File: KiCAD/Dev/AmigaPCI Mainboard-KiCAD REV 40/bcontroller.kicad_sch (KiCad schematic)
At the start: 32 parts, among them CN409 SPI, J901 IDE MODES, U111 74LVC16646, U112 74LVC16646, U409 ICE40HX4K-TQ144, U409F1 W25X20CLSN

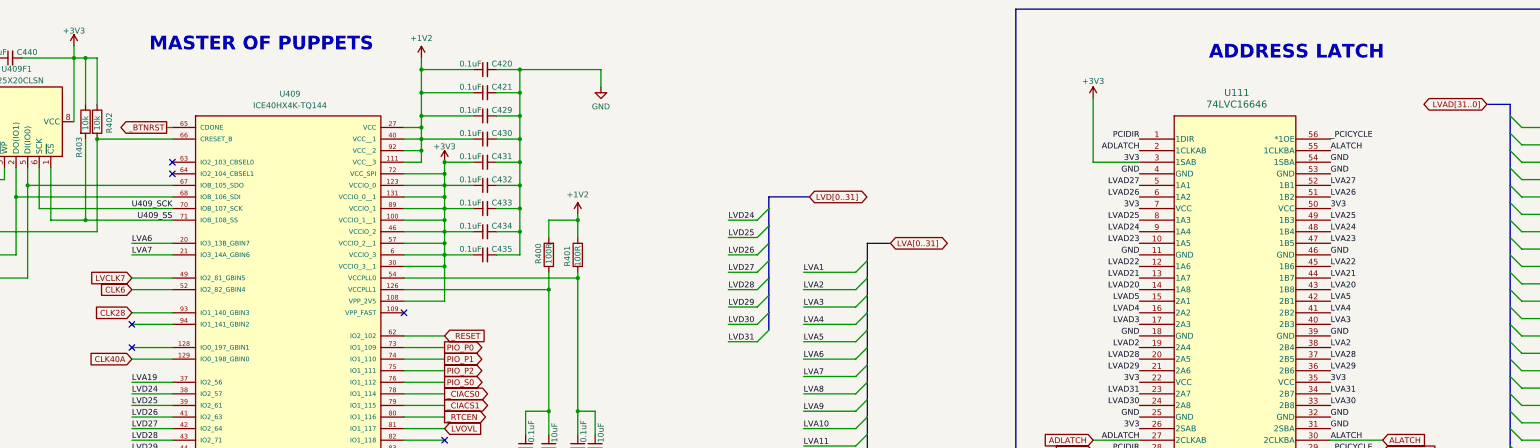
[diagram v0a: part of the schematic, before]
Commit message: Schematic Changes to Clocks 09-JUL-2024
Make changes to support clock generation on CPU local bus card.
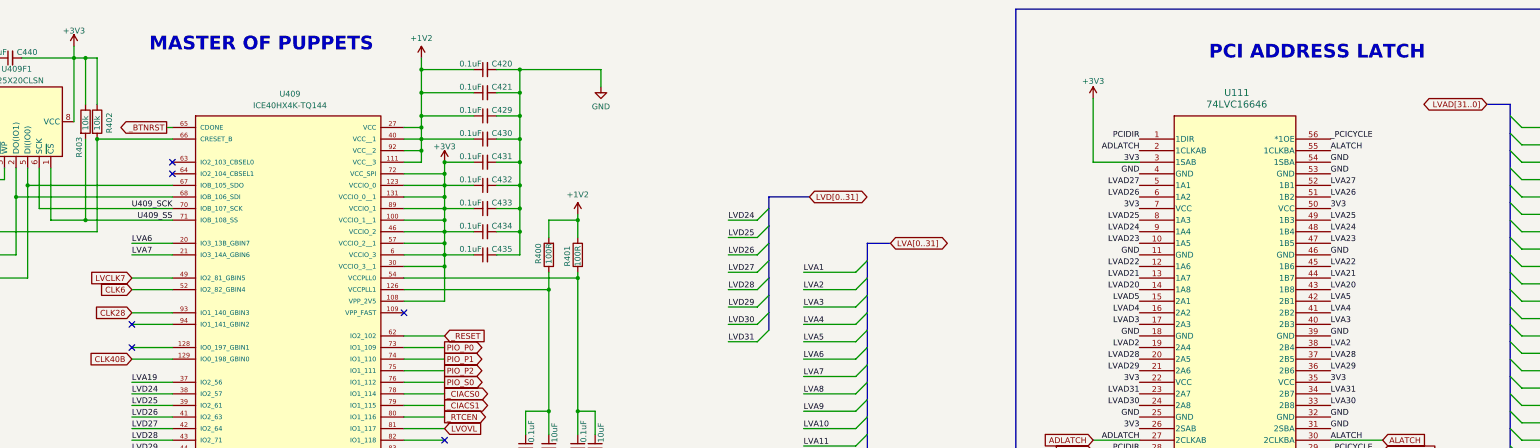
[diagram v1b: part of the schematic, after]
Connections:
- net CLK40A renamed CLK40B
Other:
- note added: "PCI ADDRESS LATCH"
- note removed: "ADDRESS LATCH"
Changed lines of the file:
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@@
 	(title_block
 		(title "AMIGA PCI")
-		(date "2024-07-03")
+		(date "2024-07-09")
 		(rev "4.0")
 	)
@@
 		)
 	)
-	(text "ADDRESS LATCH"
+	(text "PCI ADDRESS LATCH"
 		(exclude_from_sim no)
 		(at 314.96 33.528 0)
@@
 		)
 	)
-	(global_label "CLK40A"
+	(global_label "CLK40B"
 		(shape input)
 		(at 78.74 99.06 180)
@@
 		)
 		(property "Intersheetrefs" "${INTERSHEET_REFS}"
-			(at 68.6791 99.06 0)
+			(at 68.4977 99.06 0)
 			(effects
 				(font

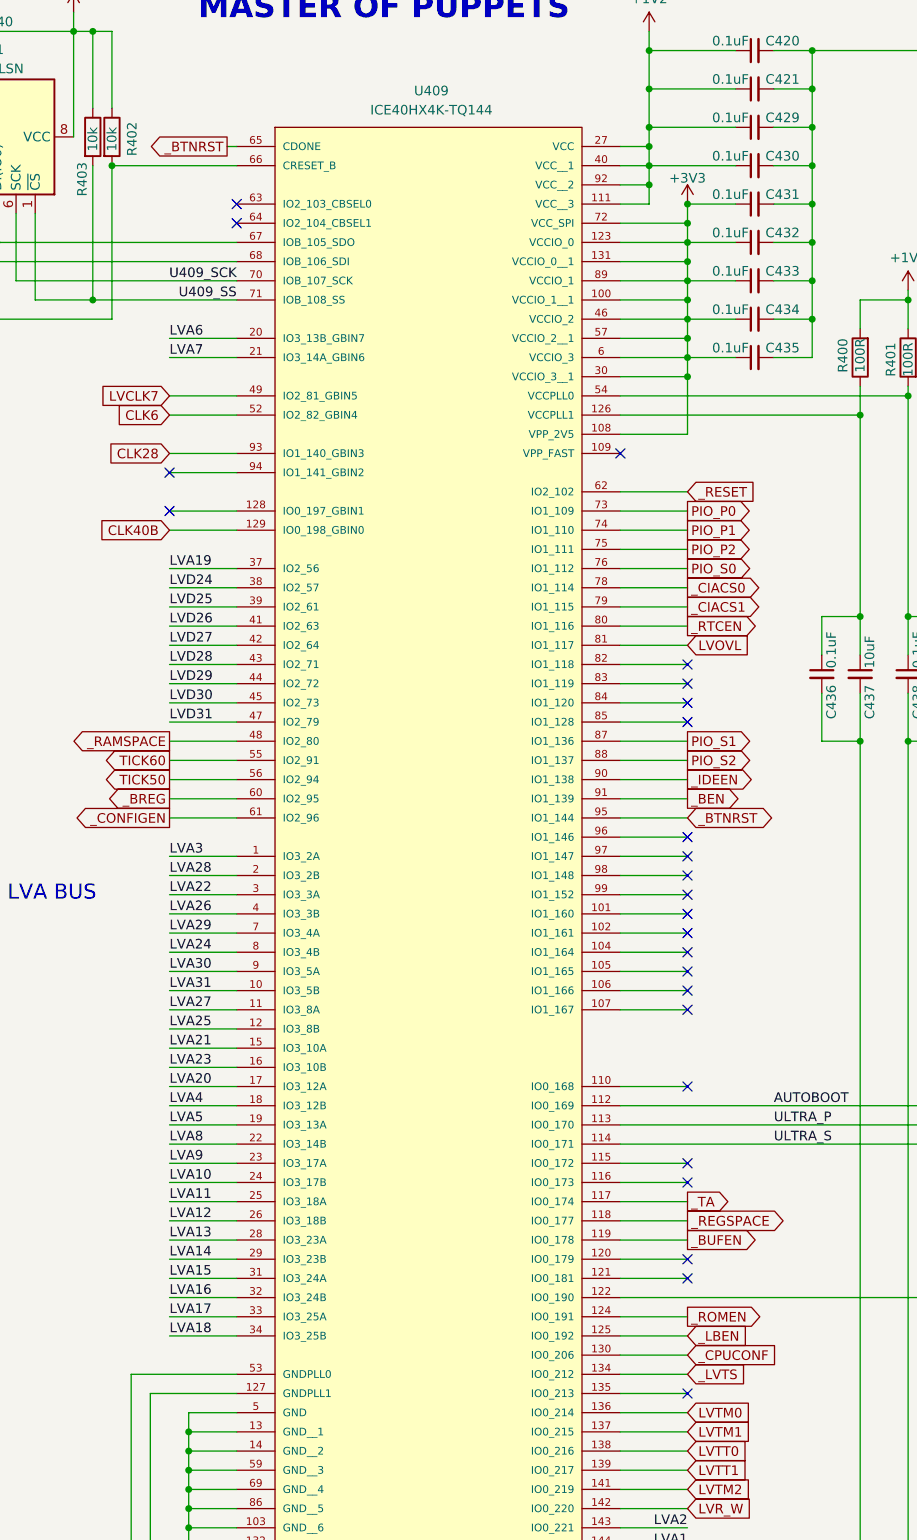
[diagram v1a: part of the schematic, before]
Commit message: AmigaPCI Rev 4.0 Schematic Updates 17-JUL-2024
Changed reset circuit, added _DSACKx, Dropped _LOCKE from Local Bus Port,  added CPU Reset In to Local Bus Port.
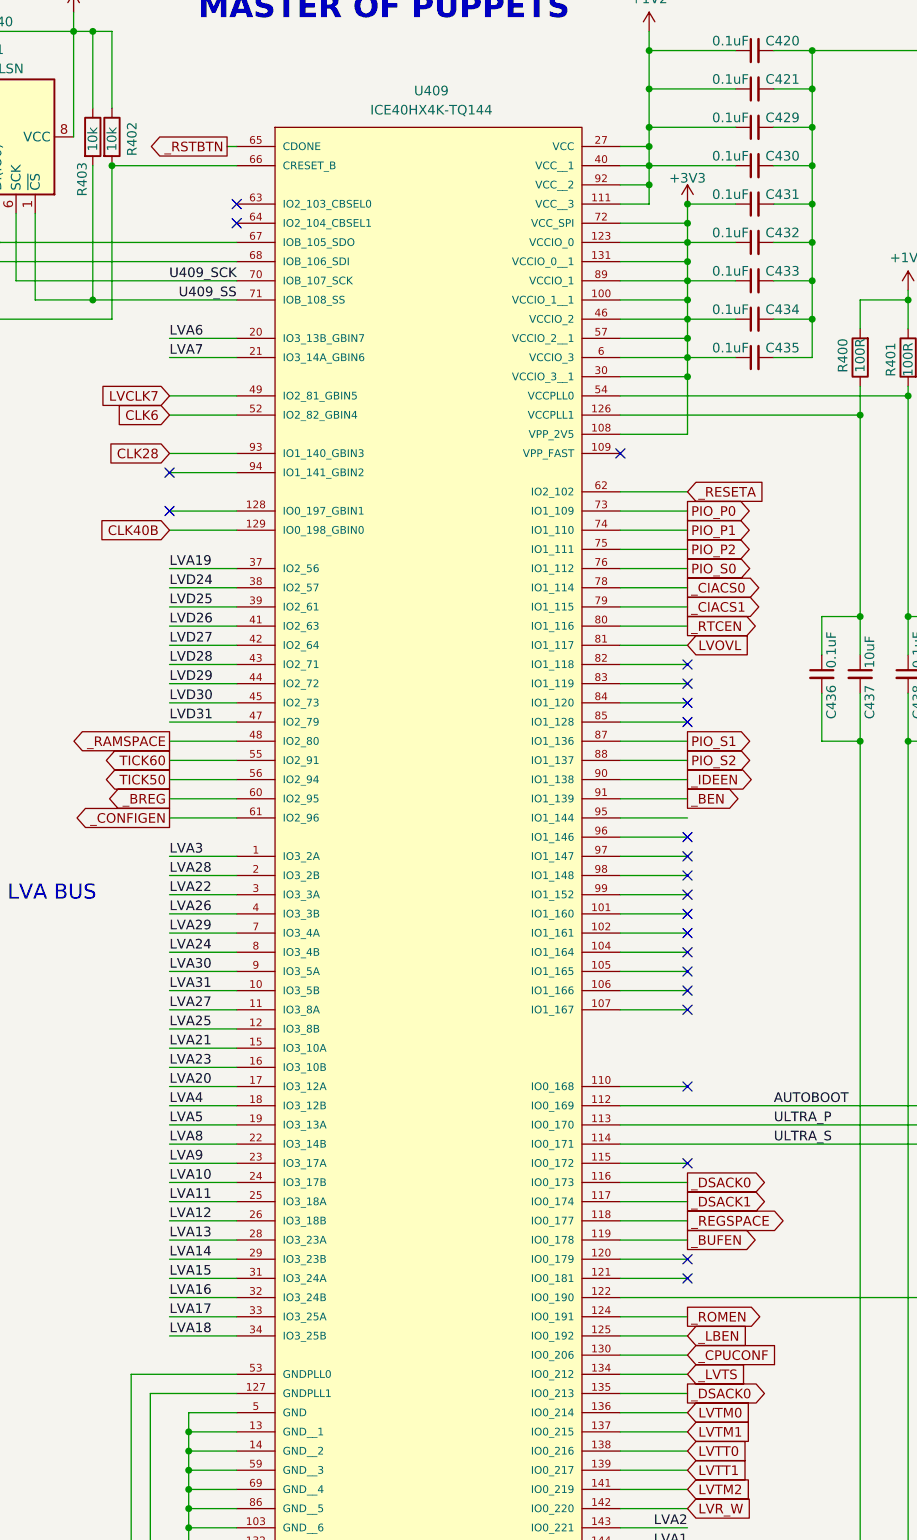
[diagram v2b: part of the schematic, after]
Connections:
- net _DSACK0: now reaches U409.116 (IO0_173)
- net _DSACK0: now also U409.135 (IO0_213)
- net _BTNRST: no longer names the net of U409.95 (IO1_144)
- net _BTNRST: no longer U409.65 (CDONE)
- net _RESET renamed _RESETA
- net _TA renamed _DSACK1
- new net _RSTBTN: U409.65 (CDONE)
- no-connect marks 29 -> 27
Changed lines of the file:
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@@
 	(title_block
 		(title "AMIGA PCI")
-		(date "2024-07-09")
+		(date "2024-07-17")
 		(rev "4.0")
 	)
@@
 	)
 	(no_connect
-		(at 147.32 185.42)
-	)
-	(no_connect
 		(at 147.32 152.4)
 	)
@@
 	)
 	(no_connect
-		(at 147.32 213.36)
-	)
-	(no_connect
 		(at 87.63 58.42)
 	)
@@
 		)
 	)
-	(global_label "_RESET"
+	(global_label "_RESETA"
 		(shape input)
 		(at 147.32 93.98 0)
@@
 		)
 	)
+	(global_label "_DSACK0"
+		(shape output)
+		(at 147.32 213.36 0)
+		(fields_autoplaced yes)
+		(effects
+			(font
+				(size 1.27 1.27)
+			)
+			(justify left)
+		)
+		(property "Intersheetrefs" "${INTERSHEET_REFS}"
+			(at 158.5904 213.36 0)
+			(effects
+				(font
+					(size 1.27 1.27)
+				)
+				(justify left)
+			)
+		)
+	)
 	(global_label "_CPUCONF"
 		(shape input)
@@
 		)
 	)
+	(global_label "_DSACK0"
+		(shape output)
+		(at 147.32 185.42 0)
+		(fields_autoplaced yes)
+		(effects
+			(font
+				(size 1.27 1.27)
+			)
+			(justify left)
+		)
+		(property "Intersheetrefs" "${INTERSHEET_REFS}"
+			(at 158.5904 185.42 0)
+			(effects
+				(font
+					(size 1.27 1.27)
+				)
+				(justify left)
+			)
+		)
+	)
 	(global_label "LVCLK7"
 		(shape input)
@@
 		)
 	)
-	(global_label "_TA"
+	(global_label "_DSACK1"
 		(shape output)
 		(at 147.32 187.96 0)
@@
 		)
 		(property "Intersheetrefs" "${INTERSHEET_REFS}"
-			(at 153.329 187.96 0)
+			(at 158.5904 187.96 0)
 			(effects
 				(font
@@
 		)
 	)
-	(global_label "_BTNRST"
-		(shape bidirectional)
-		(at 147.32 137.16 0)
-		(effects
-			(font
-				(size 1.27 1.27)
-			)
-			(justify left)
-		)
-		(property "Intersheetrefs" "${INTERSHEET_REFS}"
-			(at 158.242 137.16 0)
-			(effects
-				(font
-					(size 1.27 1.27)
-				)
-				(justify left)
-			)
-		)
-	)
 	(global_label "_IDEEN"
 		(shape output)
@@
 		)
 	)
-	(global_label "_BTNRST"
+	(global_label "_RSTBTN"
 		(shape output)
 		(at 86.36 48.26 180)

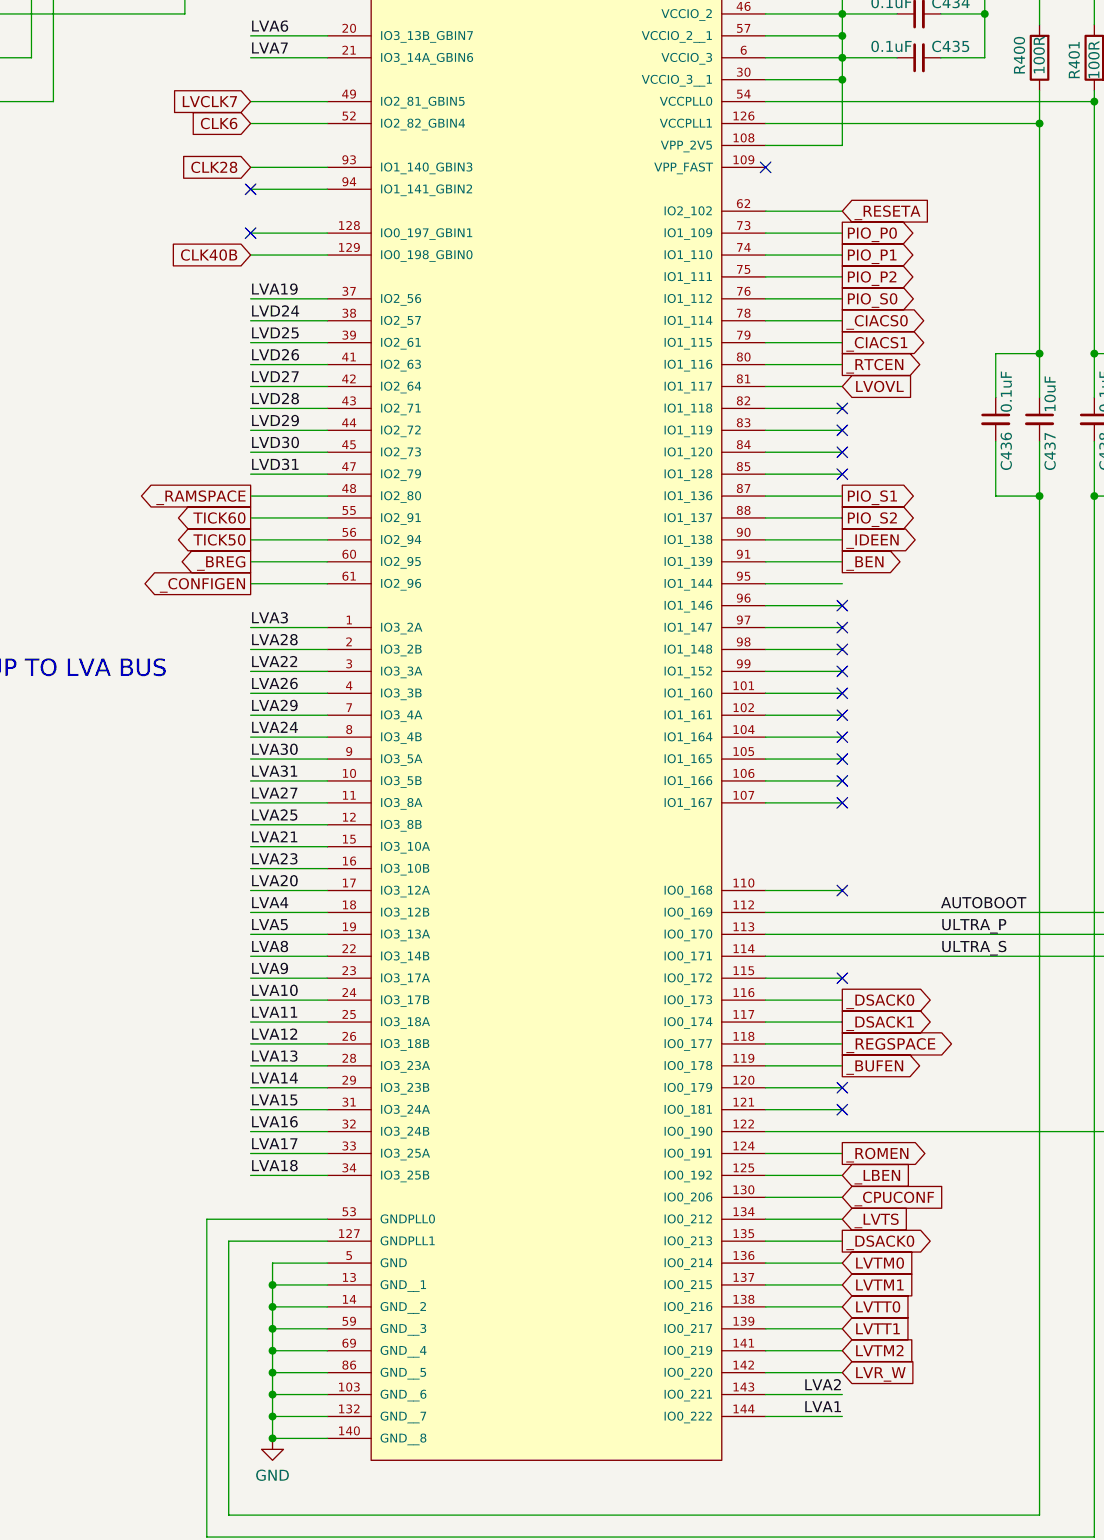
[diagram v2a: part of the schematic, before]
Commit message: AmigaPCI Rev 4.0 Routing
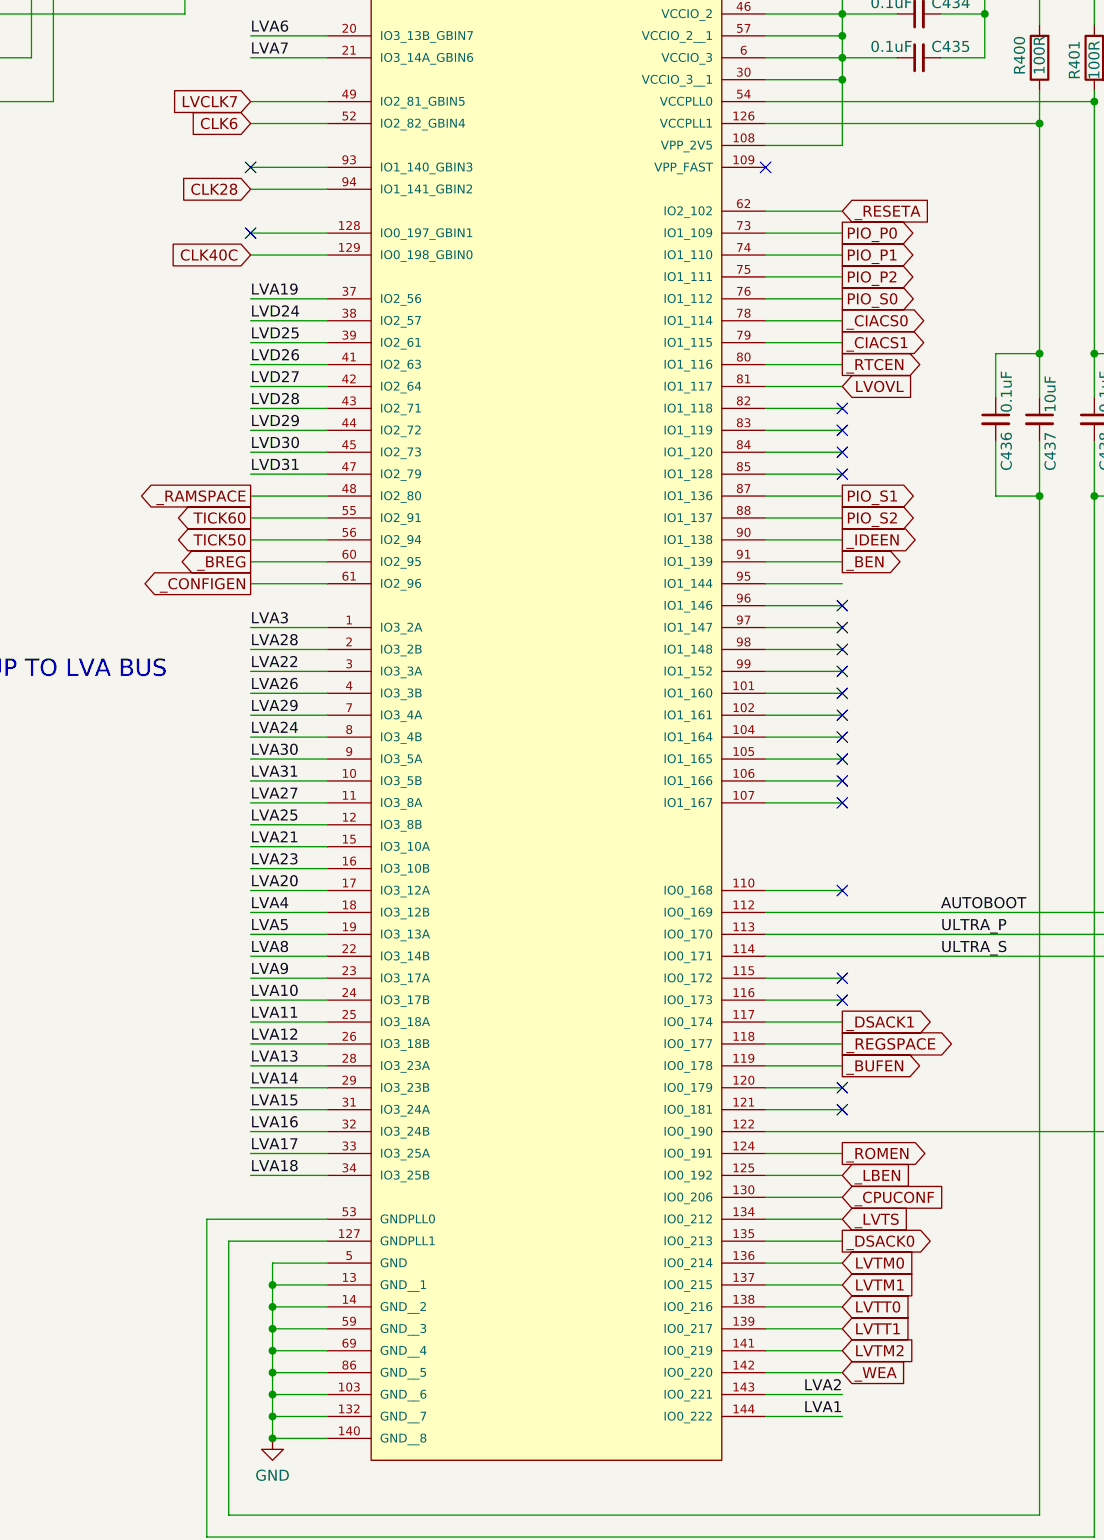
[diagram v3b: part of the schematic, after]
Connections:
- net CLK28: now also U409.94 (IO1_141_GBIN2); no longer U409.93 (IO1_140_GBIN3)
- net _DSACK0: no longer U409.116 (IO0_173)
- net CLK40B renamed CLK40C
- net LVR_W renamed _WEA
- no-connect marks 27 -> 28
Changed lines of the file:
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@@
 	)
 	(no_connect
+		(at 147.32 185.42)
+	)
+	(no_connect
 		(at 147.32 162.56)
 	)
@@
 	)
 	(no_connect
-		(at 78.74 91.44)
+		(at 78.74 88.9)
 	)
 	(no_connect
@@
 		)
 	)
-	(global_label "CLK40B"
+	(global_label "CLK40C"
 		(shape input)
 		(at 78.74 99.06 180)
@@
 		)
 	)
-	(global_label "_DSACK0"
-		(shape output)
-		(at 147.32 185.42 0)
-		(fields_autoplaced yes)
-		(effects
-			(font
-				(size 1.27 1.27)
-			)
-			(justify left)
-		)
-		(property "Intersheetrefs" "${INTERSHEET_REFS}"
-			(at 158.5904 185.42 0)
-			(effects
-				(font
-					(size 1.27 1.27)
-				)
-				(justify left)
-			)
-		)
-	)
 	(global_label "LVCLK7"
 		(shape input)
@@
 	(global_label "CLK28"
 		(shape input)
-		(at 78.74 88.9 180)
+		(at 78.74 91.44 180)
 		(fields_autoplaced yes)
 		(effects
@@
 		)
 		(property "Intersheetrefs" "${INTERSHEET_REFS}"
-			(at 69.7677 88.9 0)
+			(at 69.7677 91.44 0)
 			(effects
 				(font
@@
 		)
 	)
-	(global_label "LVR_W"
+	(global_label "_WEA"
 		(shape input)
 		(at 147.32 228.6 0)
@@
 		)
 		(property "Intersheetrefs" "${INTERSHEET_REFS}"
-			(at 156.1109 228.6 0)
+			(at 154.9618 228.6 0)
 			(effects
 				(font

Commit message: AmigaPCI Mainboard REV 4.0 Routing
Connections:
- net _TCI: now reaches U409.115 (IO0_172)
- net _TBI: now reaches U409.116 (IO0_173)
- no-connect marks 28 -> 26
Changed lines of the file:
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@@
 	(title_block
 		(title "AMIGA PCI")
-		(date "2024-07-17")
+		(date "2024-07-31")
 		(rev "4.0")
 	)
@@
 	)
 	(no_connect
-		(at 147.32 185.42)
-	)
-	(no_connect
 		(at 147.32 162.56)
 	)
@@
 	)
 	(no_connect
-		(at 147.32 182.88)
-	)
-	(no_connect
 		(at 147.32 142.24)
 	)
@@
 		)
 	)
+	(global_label "_TCI"
+		(shape output)
+		(at 147.32 182.88 0)
+		(fields_autoplaced yes)
+		(effects
+			(font
+				(size 1.27 1.27)
+			)
+			(justify left)
+		)
+		(property "Intersheetrefs" "${INTERSHEET_REFS}"
+			(at 154.1152 182.88 0)
+			(effects
+				(font
+					(size 1.27 1.27)
+				)
+				(justify left)
+			)
+		)
+	)
 	(global_label "PIO_S0"
 		(shape output)
@@
 			(effects
 				(font
+					(size 1.27 1.27)
+				)
+				(justify left)
+			)
+		)
+	)
+	(global_label "_TBI"
+		(shape output)
+		(at 147.32 185.42 0)
+		(fields_autoplaced yes)
+		(effects
+			(font
+				(size 1.27 1.27)
+			)
+			(justify left)
+		)
+		(property "Intersheetrefs" "${INTERSHEET_REFS}"
+			(at 154.1152 185.42 0)
+			(effects
+				(font
